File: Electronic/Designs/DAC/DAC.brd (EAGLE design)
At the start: 50 x 50 mm, 37 parts

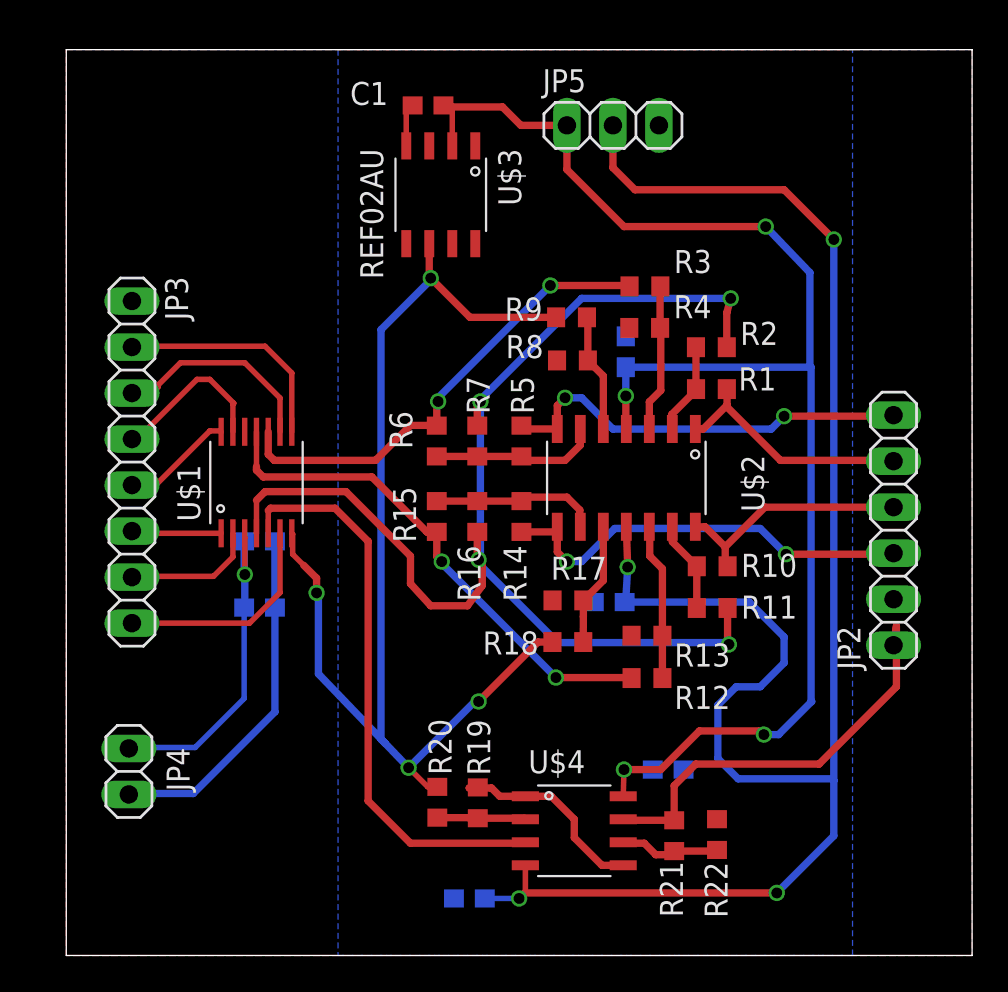
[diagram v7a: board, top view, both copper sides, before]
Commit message: Increassed isolation for ADC board, fixed DAC board isolation errors, and added mounting holes for ADC board
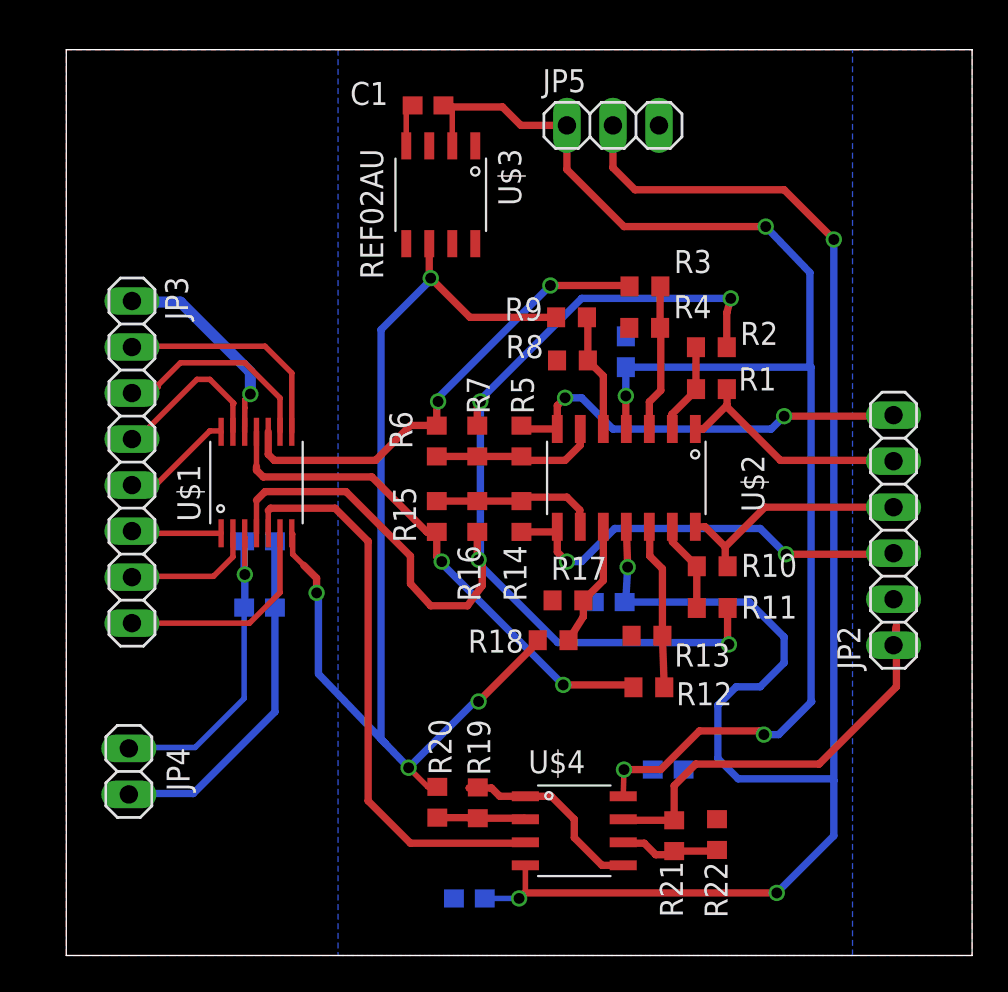
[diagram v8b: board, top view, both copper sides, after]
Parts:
- moved R18 0.82 mm to (26.9, 17.4)
- moved R12 0.52 mm to (32.2, 14.8)
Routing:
- net GND: track 22.0 -> 33.6 mm, vias 0 -> 1
- net VREF: track 65.1 -> 64.4 mm
- net N$14: track 8.65 -> 9.16 mm
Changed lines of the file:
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@@
 <attribute name="VALUE" x="35.019" y="17.2758" size="1.27" layer="27"/>
 </element>
-<element name="R12" library="resistor" package="R0603" value="10k" x="32.0548" y="15.3124" smashed="yes" rot="R180">
-<attribute name="NAME" x="36.6522" y="14.8806" size="1.27" layer="25" rot="R180"/>
-<attribute name="VALUE" x="32.6898" y="17.2174" size="1.27" layer="27" rot="R180"/>
+<element name="R12" library="resistor" package="R0603" value="10k" x="32.1564" y="14.8044" smashed="yes" rot="R180">
+<attribute name="NAME" x="36.7538" y="15.0838" size="1.27" layer="25" rot="R180"/>
+<attribute name="VALUE" x="32.7914" y="16.7094" size="1.27" layer="27" rot="R180"/>
 </element>
 <element name="R13" library="resistor" package="R0603" value="40k" x="32.0548" y="17.6492" smashed="yes" rot="R180">
@@
 <attribute name="VALUE" x="27.0566" y="17.6954" size="1.27" layer="27"/>
 </element>
-<element name="R18" library="resistor" package="R0603" value="10k" x="27.686" y="17.3012" smashed="yes">
-<attribute name="NAME" x="22.987" y="16.6154" size="1.27" layer="25"/>
-<attribute name="VALUE" x="27.051" y="15.3962" size="1.27" layer="27"/>
+<element name="R18" library="resistor" package="R0603" value="10k" x="26.8732" y="17.4028" smashed="yes">
+<attribute name="NAME" x="22.1742" y="16.717" size="1.27" layer="25"/>
+<attribute name="VALUE" x="26.2382" y="15.4978" size="1.27" layer="27"/>
 </element>
 <element name="R2" library="resistor" package="R0603" value="10k" x="35.6076" y="33.5764" smashed="yes" rot="R180">
@@
 </polygon>
 <contactref element="JP2" pad="2"/>
-<wire x1="11.518" y1="22.86" x2="9.8484" y2="28.9056" width="0" layer="19" extent="1-16"/>
+<wire x1="9.8484" y1="28.9056" x2="9.8552" y2="30.2264" width="0.3048" layer="1"/>
+<via x="10.16" y="30.988" extent="1-16" drill="0.6"/>
+<wire x1="10.16" y1="30.988" x2="10.16" y2="32.2072" width="0.6096" layer="16"/>
+<wire x1="10.16" y1="32.2072" x2="6.2992" y2="36.068" width="0.6096" layer="16"/>
+<wire x1="6.2992" y1="36.068" x2="3.6828" y2="36.068" width="0.6096" layer="16"/>
+<wire x1="3.6828" y1="36.068" x2="3.6256" y2="36.1252" width="0.3048" layer="16"/>
+<wire x1="9.8552" y1="30.2264" x2="9.8552" y2="30.6832" width="0.3048" layer="1"/>
+<wire x1="9.8552" y1="30.6832" x2="10.16" y2="30.988" width="0.3048" layer="1"/>
 <wire x1="31.0768" y1="34.642" x2="30.8864" y2="34.1748" width="0" layer="19" extent="1-16"/>
-<wire x1="31.2048" y1="17.6492" x2="29.122" y2="19.5072" width="0" layer="19" extent="1-16"/>
 </signal>
 <signal name="XPOS">
@@
 <wire x1="27.0392" y1="35.226" x2="22.2796" y2="35.226" width="0.4064" layer="1"/>
 <wire x1="22.2796" y1="35.226" x2="20.1168" y2="37.3888" width="0.4064" layer="1"/>
-<wire x1="26.836" y1="17.3012" x2="26.0388" y2="17.3012" width="0.4064" layer="1"/>
+<wire x1="26.0232" y1="17.4028" x2="26.0388" y2="17.3012" width="0.4064" layer="1"/>
 <wire x1="26.0388" y1="17.3012" x2="22.7584" y2="14.0208" width="0.4064" layer="1"/>
 <via x="22.7584" y="14.0208" extent="1-16" drill="0.6"/>
@@
 <wire x1="32.2072" y1="22.0472" x2="32.2072" y2="23.6388" width="0.4064" layer="1"/>
 <wire x1="32.2072" y1="23.6388" x2="32.1836" y2="23.6624" width="0.4064" layer="1"/>
-<wire x1="32.9048" y1="15.3124" x2="32.9048" y2="17.6492" width="0.4064" layer="1"/>
+<wire x1="33.0064" y1="14.8044" x2="32.9048" y2="17.6492" width="0.4064" layer="1"/>
 </signal>
 <signal name="N$16">
@@
 <via x="20.7264" y="21.7424" extent="1-16" drill="0.6"/>
 <wire x1="20.7264" y1="21.7424" x2="20.7264" y2="21.6408" width="0.4064" layer="16"/>
-<wire x1="20.7264" y1="21.6408" x2="27.0256" y2="15.3416" width="0.4064" layer="16"/>
-<via x="27.0256" y="15.3416" extent="1-16" drill="0.6"/>
-<wire x1="27.0256" y1="15.3416" x2="31.1756" y2="15.3416" width="0.4064" layer="1"/>
-<wire x1="31.1756" y1="15.3416" x2="31.2048" y2="15.3124" width="0.4064" layer="1"/>
+<wire x1="20.7264" y1="21.6408" x2="27.432" y2="14.9352" width="0.4064" layer="16"/>
+<via x="27.432" y="14.9352" extent="1-16" drill="0.6"/>
+<wire x1="27.432" y1="14.9352" x2="31.2772" y2="14.9352" width="0.4064" layer="1"/>
+<wire x1="31.2772" y1="14.9352" x2="31.3064" y2="14.8044" width="0.4064" layer="1"/>
 <wire x1="16.8656" y1="26.416" x2="19.9136" y2="23.368" width="0.4064" layer="1"/>
 <wire x1="19.9136" y1="23.368" x2="20.4372" y2="23.368" width="0.4064" layer="1"/>
@@
 <wire x1="29.6436" y1="20.7024" x2="28.5416" y2="19.6004" width="0.4064" layer="1"/>
 <wire x1="28.5416" y1="19.6004" x2="28.5416" y2="18.702" width="0.4064" layer="1"/>
-<wire x1="28.5416" y1="18.702" x2="28.536" y2="17.3012" width="0.4064" layer="1"/>
+<wire x1="28.5416" y1="18.702" x2="27.7232" y2="17.4028" width="0.4064" layer="1"/>
 </signal>
 <signal name="B">
